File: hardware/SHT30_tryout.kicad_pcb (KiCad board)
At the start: 2 copper layers, 6 parts, among them J1 SHT3x_HEADER, U1 VAL**

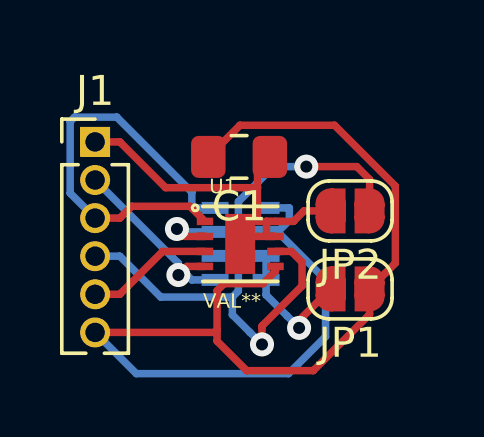
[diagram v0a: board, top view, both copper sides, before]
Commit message: update for pin assignment,
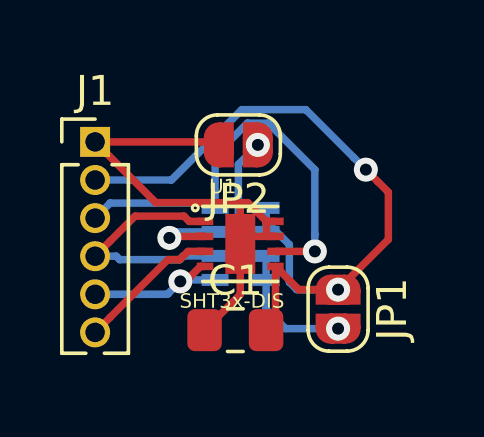
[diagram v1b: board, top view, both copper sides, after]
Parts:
- JP1: value SolderJumper_2_Open_round -> SCL_SDA
- U1: value VAL** -> SHT3x-DIS
- moved C1 5.78 mm to (29.2, 28.9), turned to 0 degrees
- moved JP2 4.33 mm to (29.3, 22.7)
- moved JP1 0.78 mm to (32.6, 28.2), turned to 270 degrees
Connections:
- J1 pad 2: /SCL -> +3V3
- J1 pad 3: /SDA -> /NRST
- J1 pad 4: /NRST -> /SDA
- J1 pad 5: /ALERT -> /SCL
- J1 pad 6: +3V3 -> /ALERT
- RN1 pad 2: /NRST -> /SDA
- RN1 pad 4: /SDA -> /NRST
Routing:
- net +3V3: track 41.6 -> 25.8 mm, vias 0 -> 2
- net /SDA: track 14.1 -> 8.39 mm
- net GND: track 12.7 -> 17.8 mm
- net /ADDR: track 10.2 -> 6.72 mm
- net /SCL: track 6.61 -> 5.23 mm
- net /NRST: track 13.7 -> 14.5 mm
- net /ALERT: track 4.26 -> 4.78 mm
